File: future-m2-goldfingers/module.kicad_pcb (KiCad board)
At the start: 4 copper layers, 22 x 42 mm, 44 parts, among them J1 M.2 Key M card edge (custom p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, J3 U.FL-R-SMT-1(01), U1 ESP32-C6FH8, U2 iCE40UP5K-SG48, U3 TLV75512PDBVR, Y1 40MHz / CL10pF

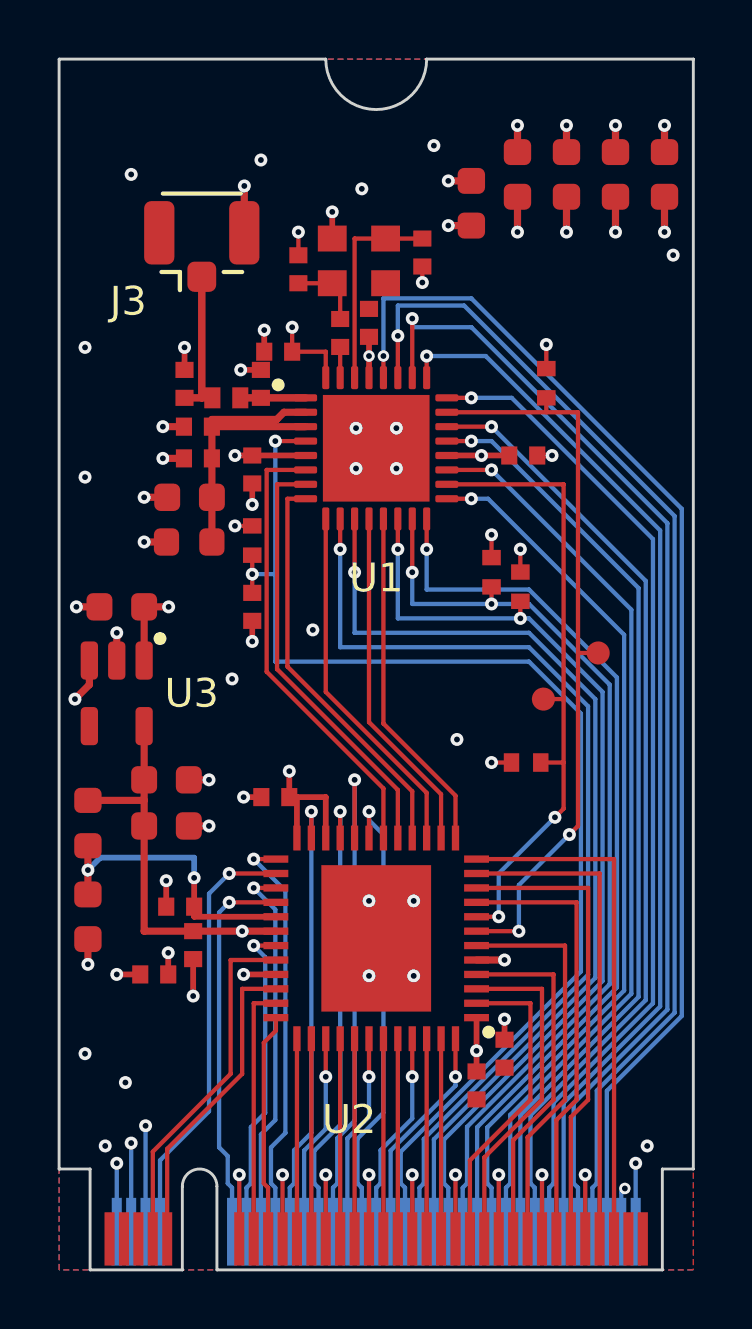
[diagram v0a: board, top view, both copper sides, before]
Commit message: Bring C38 and C49 onto their supply pins
C38 (ESP VDDPST2, pin 20) moves 0.2 mm west to 1.97 mm by swapping the GPIO15 and USB D+ via drops
and nudging the pin-20 plane via. C49 (FPGA core VCC, pin 30) now lies on the pin-30 line at 1.94 mm;
the 1.2 V regulator trunk enters the inner-layer island through a new west lobe instead of a front
track past the cap, and the PLL pin line narrows to 0.15 mm beside it.

The remaining four cases (U2 pins 5, 29, 33 and ESP VDDA3P3) are boxed in by I/O exits on both
sides of the pin at 0.5 mm pitch; the contract and README record the per-pin reason.

ERC 0, DRC with parity 0/0, lint info-only (22), quality decoupling findings 9 -> 7.

Co-Authored-By: Claude Fable 5.1 <noreply@anthropic.com>
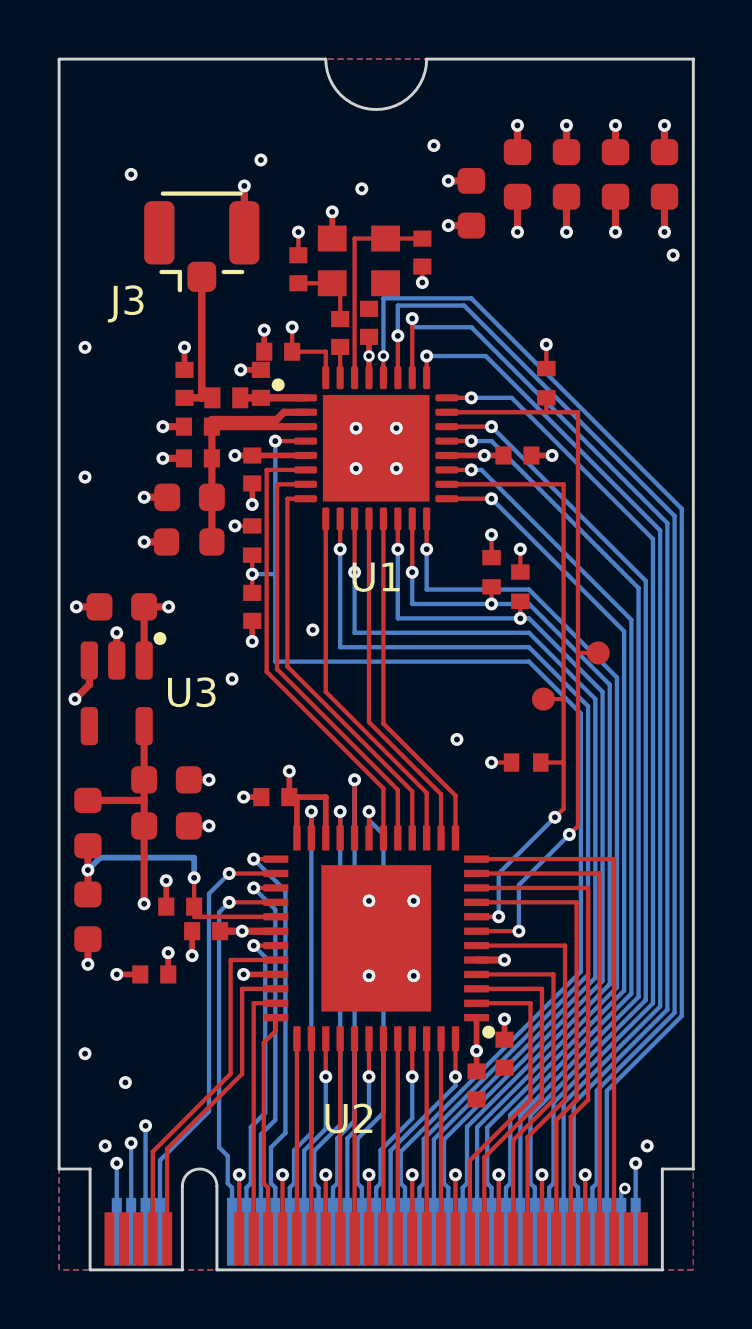
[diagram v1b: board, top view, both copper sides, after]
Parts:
- moved C49 0.66 mm to (105.1, 130.2), turned to 180 degrees
- moved C38 0.20 mm to (115.9, 113.8)
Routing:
- net +1.2V: track 15.3 -> 11.7 mm, vias 3 -> 4

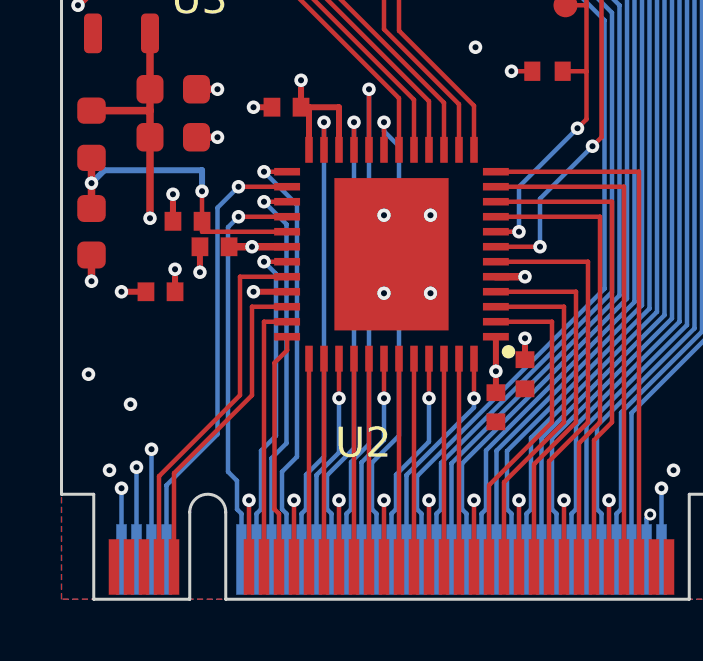
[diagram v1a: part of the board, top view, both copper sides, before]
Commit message: Stagger the U2 west via drops into a tight zig-zag
Pins 25-33 now alternate between two via columns 0.55 mm apart
(x 106.75 / 106.2): 25 A, 26 B, 27 A, 28 B, 30 A (island feed), 31 B,
33 A (plane via). Pin 31 lanes west on x 105.9 and re-enters contact 56
with a south-east leg; the +1.2V island wall moves to x 107.3 so the
pin-33 plane via stays in the +3.3V plane.

ERC 0, DRC with parity 0, lint 22 infos (unchanged), quality unchanged.

Co-Authored-By: Claude Fable 5.1 <noreply@anthropic.com>
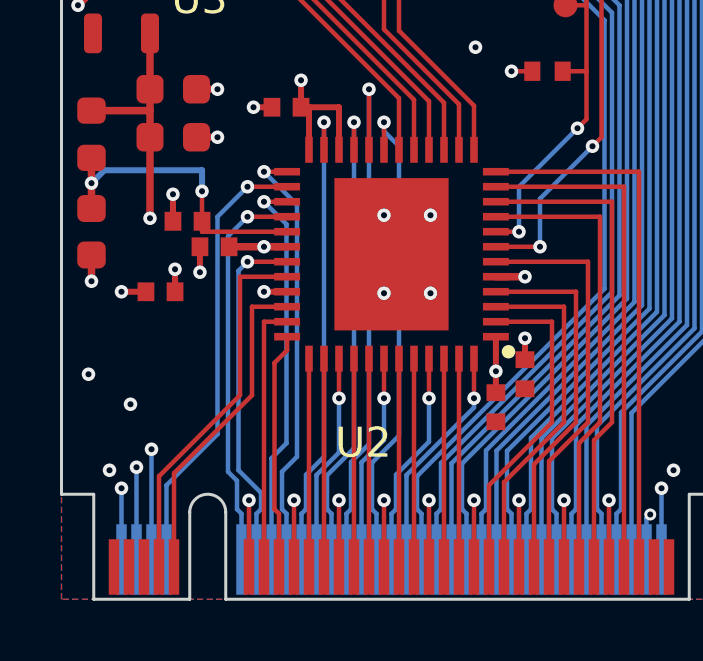
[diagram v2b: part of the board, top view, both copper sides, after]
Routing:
- net FPGA_IOT_42B: track 11.1 -> 11.7 mm

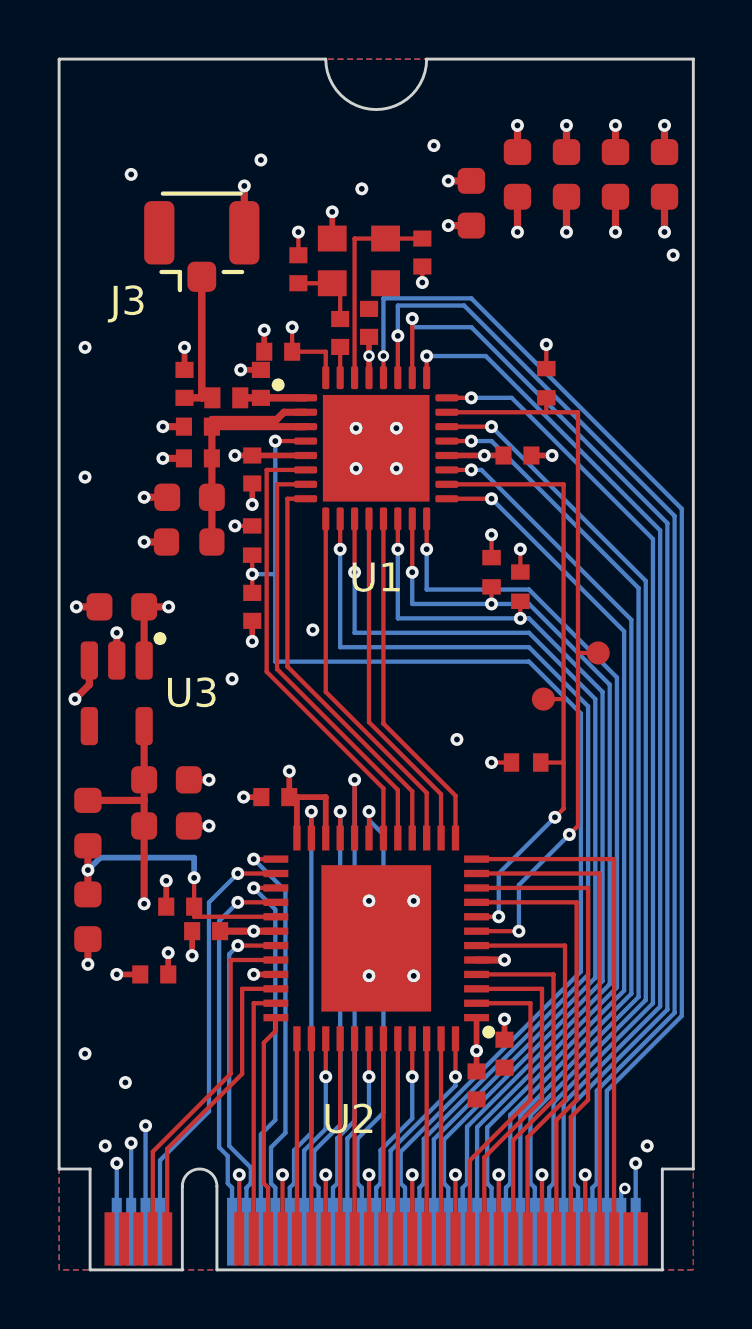
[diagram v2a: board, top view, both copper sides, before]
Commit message: Meet the JLCPCB gold-finger rules on the M.2 card edge
Per https://jlcpcb.com/help/article/jlcpcb-gold-fingers (read 2026-10-07):
- fingers stop 0.6 mm inside the routed edge (their 30 degree bevel
  copper setback, 1.13 mm at 1.6 mm, scaled to the 0.8 mm card and
  rounded up); the inner pad ends stay at 2.0 / 2.5 mm;
- one solder-mask window per side over the whole finger field, with
  mask bridges allowed on J1 and a rule area that keeps the pours out;
- the end ground contacts 1/3 and 71/73/75, which used to join the
  pour, now run to the board-end vias on hand-drawn tracks;
- fab notes, README and contract record ENIG + gold-finger option,
  30 degree bevel, and the >= 50 x 50 mm panel requirement (connector
  edge on the panel outline, no V-cut through the fingers).

ERC 0, DRC with parity 0, lint 22 infos (unchanged), quality unchanged.

Co-Authored-By: Claude Fable 5.1 <noreply@anthropic.com>
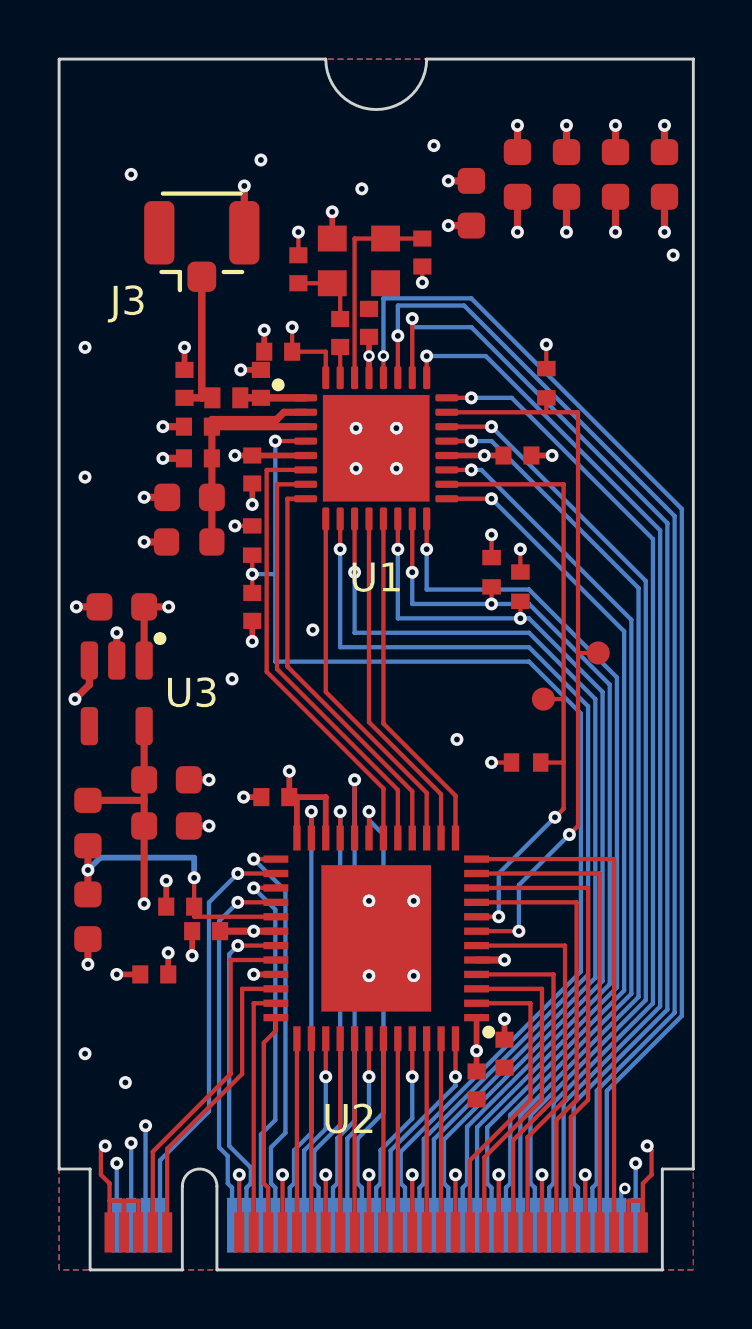
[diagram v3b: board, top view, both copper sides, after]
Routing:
- net GND: track 43.0 -> 52.1 mm
- net +3.3V: track 43.9 -> 42.8 mm
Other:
- board text added: "Card edge: ENIG + gold fingers, 30 deg bevel (copper setback 0.6 mm, mask open); PCB 0.80 +/-0.08 mm; M.2 2242 key M"
- board text added: "Order as a panel >= 50 x 50 mm with this edge on the panel outline (no V-cut through the fingers)"
- board text removed: "Card edge: 20 deg bevel, 0.30 mm; hard gold on fingers; PCB 0.80 +/-0.08 mm; M.2 2242 key M"

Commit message: Miter the nested ESP feeder corners and deepen their lane legs
ESP_EN, GPIO4, GPIO5, GPIO8, GPIO9_BOOT and USB_D- each get a 0.8 mm
45-degree corner off the via drop instead of a square turn. Their legs
into the B.Cu lanes now start further west (x 115.7 .. 116.2) and step
0.6 mm in y - x, set by GPIO8's in-line R21 via at x 116.0.

ERC 0, DRC with parity 0, lint 24 infos (route.bend_count +2 from the
added miters), quality unchanged.

Co-Authored-By: Claude Opus 5.5 <noreply@anthropic.com>
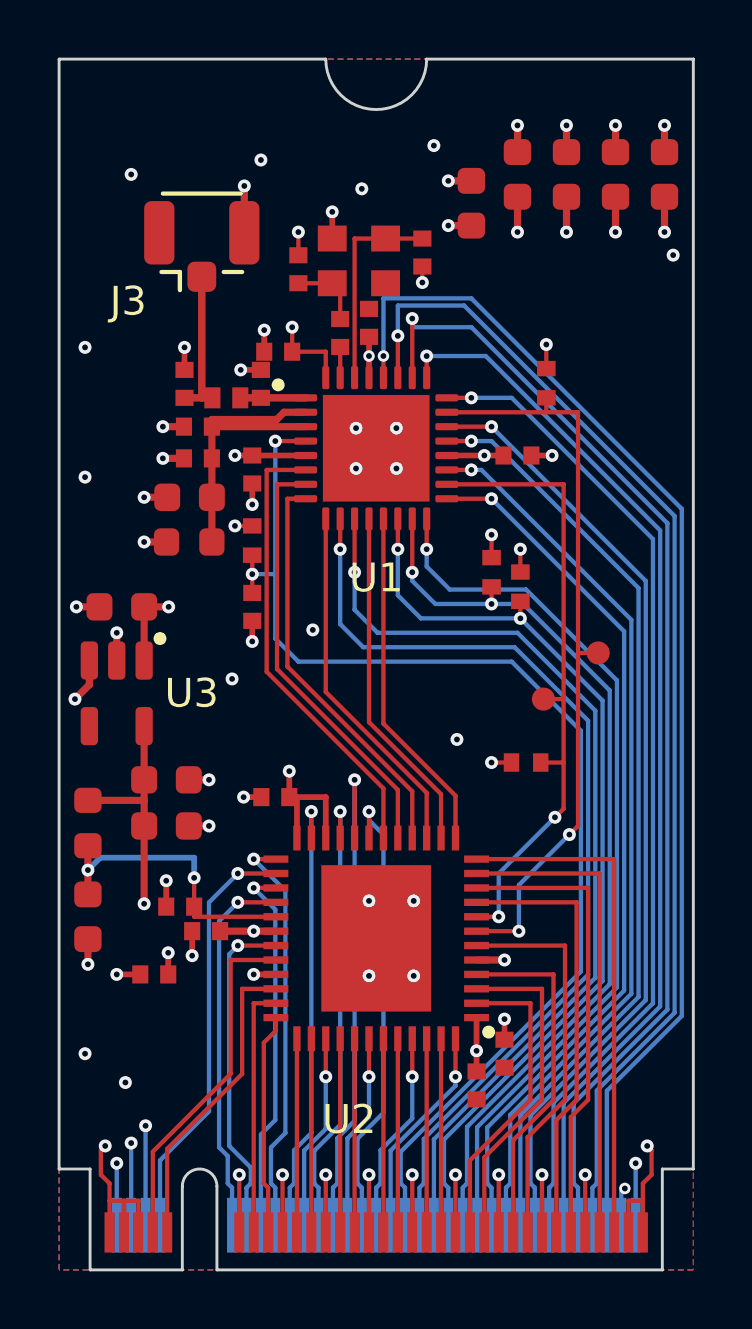
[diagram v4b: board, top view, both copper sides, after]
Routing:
- net ESP_EN: track 42.6 -> 41.7 mm
- net ESP_GPIO4: track 34.3 -> 33.6 mm
- net ESP_GPIO5: track 33.8 -> 33.1 mm
- net ESP_GPIO8: track 33.0 -> 32.4 mm
- net ESP_GPIO9_BOOT: track 32.4 -> 31.8 mm
- net USB_D-: track 31.3 -> 30.8 mm
